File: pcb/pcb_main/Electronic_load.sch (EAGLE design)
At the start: 112 parts, among them IC7 LM1117IMPX-5.0, J1 XT60-M, J2 B2B-XH, J3 B4B-XH, J4 B2B-XH, J5 B2B-XH, J6 B2B-XH, J7 B2B-XH, J8 B5B-XH, Q1 IRFP250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

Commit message: poormans rebase xd (im tired...)
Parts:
- R22: value 1k -> 560R
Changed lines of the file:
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@@
 <part name="VDD1" library="supply1" library_urn="urn:adsk.eagle:library:371" deviceset="VDD" device=""/>
 <part name="R21" library="rcl" library_urn="urn:adsk.eagle:library:334" deviceset="R-EU_" device="R0603" package3d_urn="urn:adsk.eagle:package:23555/3" value="10k"/>
-<part name="R22" library="rcl" library_urn="urn:adsk.eagle:library:334" deviceset="R-EU_" device="R0603" package3d_urn="urn:adsk.eagle:package:23555/3" value="1k"/>
+<part name="R22" library="rcl" library_urn="urn:adsk.eagle:library:334" deviceset="R-EU_" device="R0603" package3d_urn="urn:adsk.eagle:package:23555/3" value="560R"/>
 <part name="C5" library="rcl" library_urn="urn:adsk.eagle:library:334" deviceset="C-EU" device="C0603" package3d_urn="urn:adsk.eagle:package:23616/2" value="1n"/>
 <part name="GND3" library="supply1" library_urn="urn:adsk.eagle:library:371" deviceset="GND" device=""/>

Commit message: Add missing component designators on schematic, adjust text size and positioning
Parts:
- U5: value OPA277-SOIC08 -> OPA277
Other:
- note added: "Note: Desolder the I2C pull-up resistors from the LCD I2C converter module."
- note removed: "Note: desolder pull-up resistors on LCD I2C module"
- moved on the sheet: C10, C11, C12, C13, C26, C27, C5, C7, C8, C9, D1, D2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

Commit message: Improve schematic, adjust text size and positioning
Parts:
- IC7: value LM1117IMPX-5.0 -> LM1117-5.0
- U$2: value CRYSTAL_3,4X2,7 -> 16MHz
- VR1: value (none) -> TL431
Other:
- note added: "Power stage"
- note removed: "Power electronics"
- moved on the sheet: C13, C14, C15, C16, C23, C26, C27, C5, C7, C8, C9, D5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

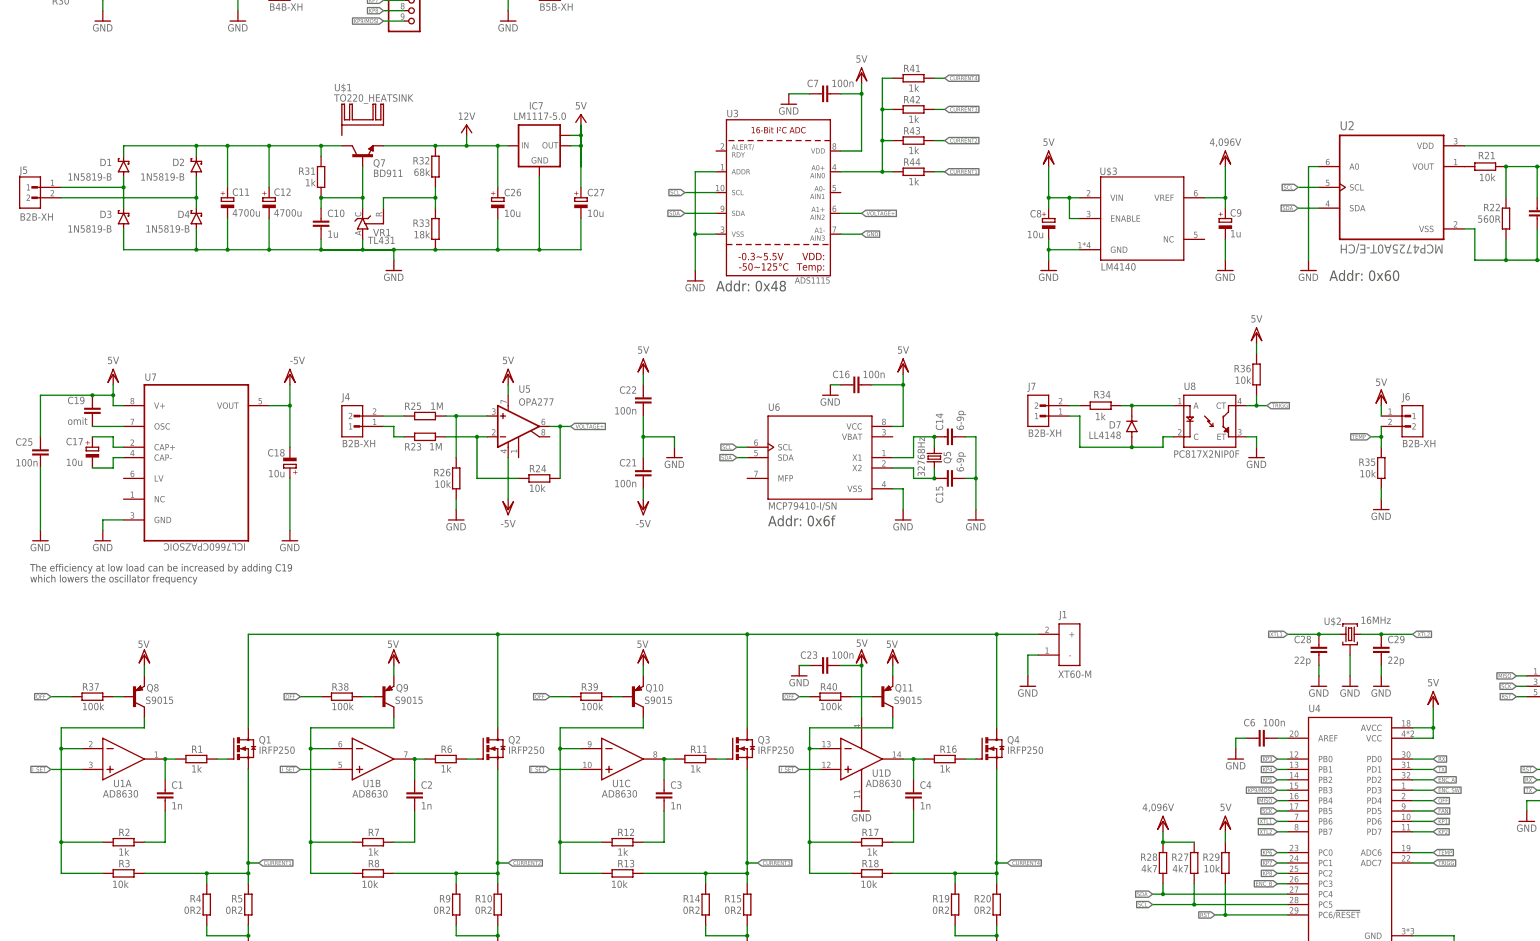
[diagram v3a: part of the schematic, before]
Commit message: Rename CURRENTx nets to V_SHUNT_x, add negation to OFF net on the main pcb
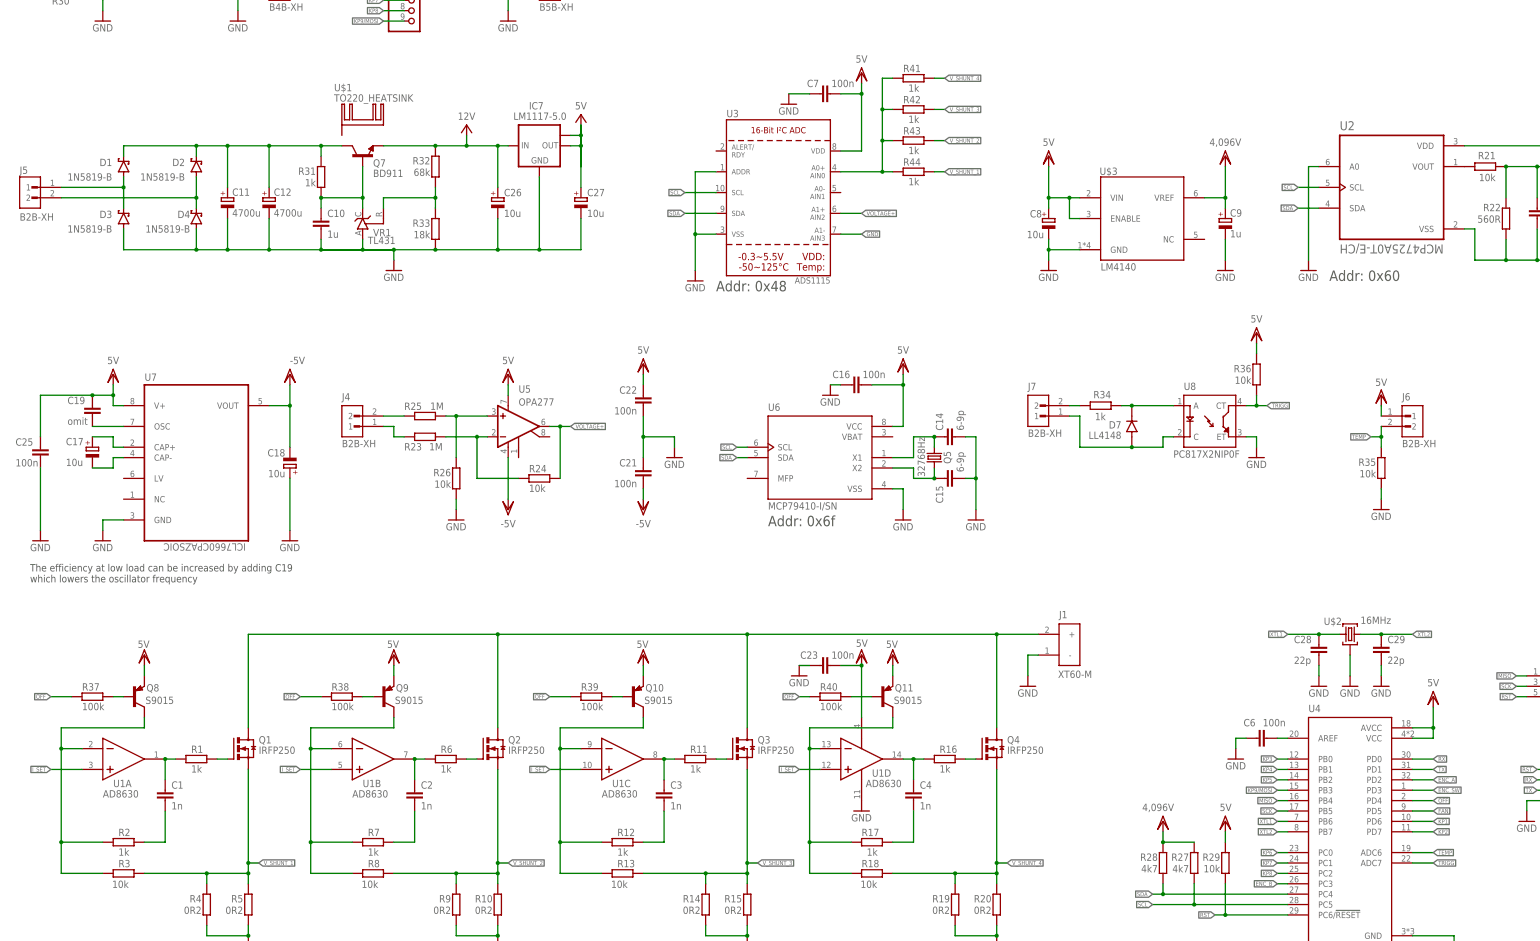
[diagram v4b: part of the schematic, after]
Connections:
- net CURRENT1 renamed V_SHUNT_1
- net CURRENT2 renamed V_SHUNT_2
- net CURRENT3 renamed V_SHUNT_3
- net CURRENT4 renamed V_SHUNT_4
- net OFF renamed !OFF
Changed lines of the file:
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@@
 </segment>
 </net>
-<net name="CURRENT1" class="0">
+<net name="V_SHUNT_1" class="0">
 <segment>
 <pinref part="Q1" gate="G$1" pin="S"/>
@@
 </segment>
 </net>
-<net name="CURRENT2" class="0">
+<net name="V_SHUNT_2" class="0">
 <segment>
 <pinref part="Q2" gate="G$1" pin="S"/>
@@
 </segment>
 </net>
-<net name="CURRENT3" class="0">
+<net name="V_SHUNT_3" class="0">
 <segment>
 <pinref part="Q3" gate="G$1" pin="S"/>
@@
 </segment>
 </net>
-<net name="CURRENT4" class="0">
+<net name="V_SHUNT_4" class="0">
 <segment>
 <pinref part="Q4" gate="G$1" pin="S"/>
@@
 </segment>
 </net>
-<net name="OFF" class="0">
+<net name="!OFF" class="0">
 <segment>
 <pinref part="R37" gate="G$1" pin="1"/>
